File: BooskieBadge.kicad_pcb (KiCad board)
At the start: 2 copper layers, 53 parts, among them J1 TC2030, J2 SFV24R-2STE1HLF, Q1 Si1308EDL, U1 nRF52840, Y1 32MHz

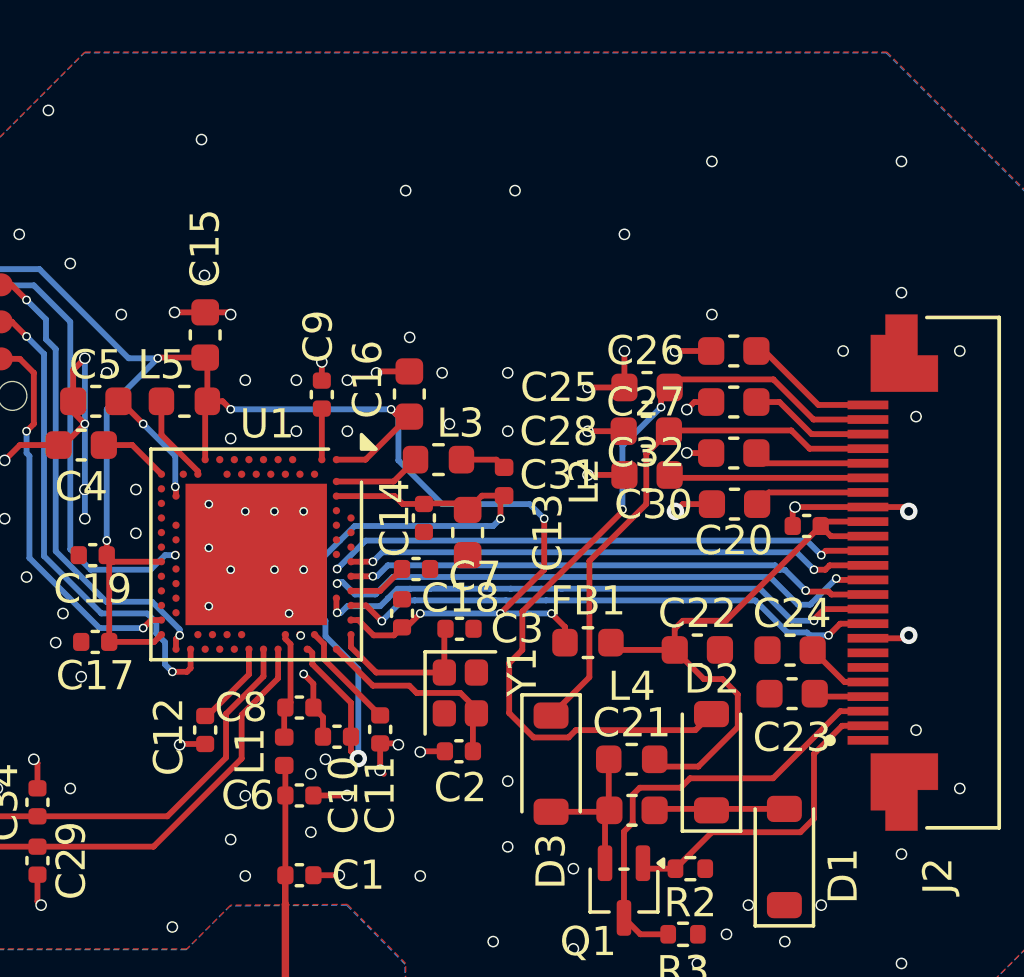
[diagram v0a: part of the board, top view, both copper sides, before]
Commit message: cleaned up some grounds
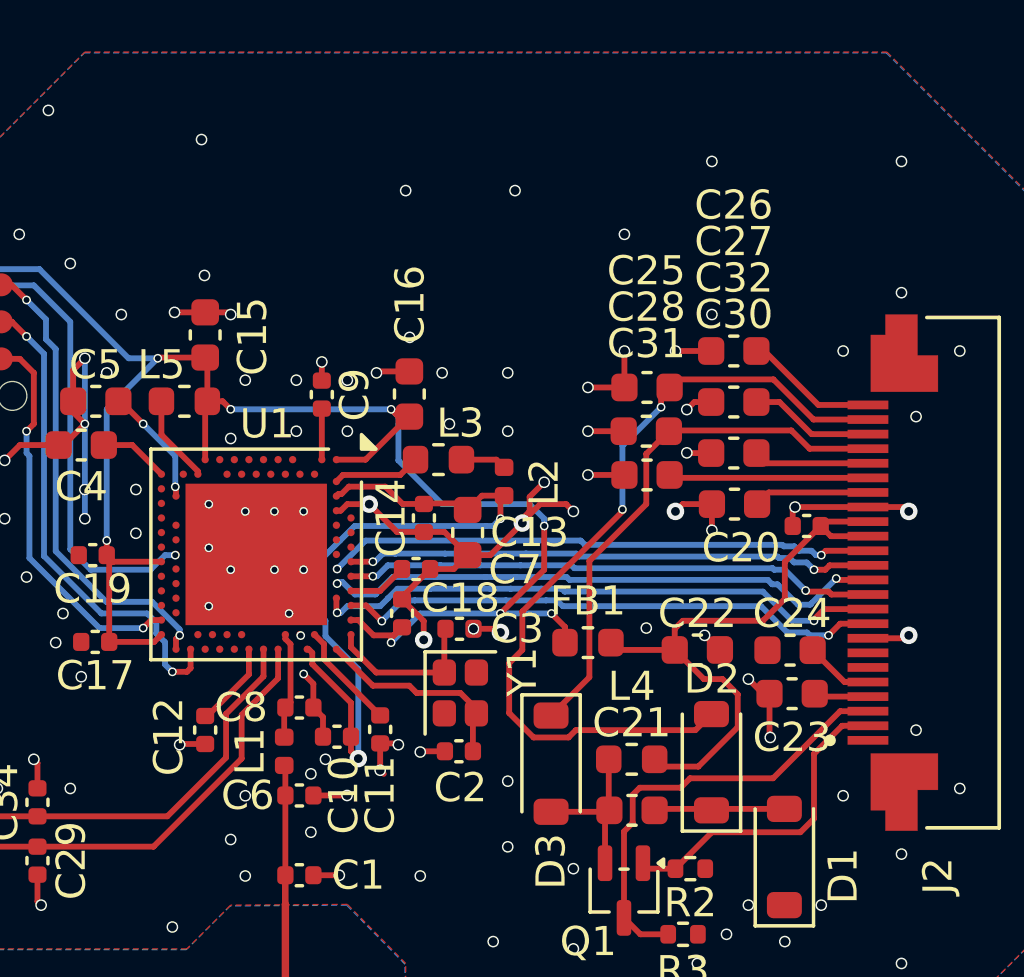
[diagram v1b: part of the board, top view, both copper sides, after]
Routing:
- net GND: track 46.4 -> 67.6 mm, vias 109 -> 122
- net VDD: track 58.9 -> 60.1 mm
- net +3V3: track 20.3 -> 21.0 mm

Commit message: screwing around with ports and stuff
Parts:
- added BT1: Battery_Cell, BooskieBadge:BAT_HOLDER_2032SMD, F.Cu at (97.0, 154.1)
- added J3: USB_C_Receptacle_PCB_Edge, BooskieBadge:USB_C_PCB_receptacle_24pin_1mm-cutout, F.Cu at (107.8, 119.3)
- added J4: USB_A_PCB_Edge_receptacle, BooskieBadge:USB_A_PCB_Edge_receptacle, F.Cu at (92.8, 120.8)
- added R1: 5.1k, Resistor_SMD:R_0402_1005Metric, F.Cu at (103.7, 125.3)
- added R4: 5.1k, Resistor_SMD:R_0402_1005Metric, F.Cu at (103.7, 127.2)
- added U2: USBLC6-2P6, Package_TO_SOT_SMD:SOT-666, F.Cu at (89.3, 129.2)
- added U3: SAOV1.69BIS, BooskieBadge:Simple_Addon_v2-BADGE-2x3, F.Cu at (127.2, 124.0)
- moved AE2 10.3 mm to (90.0, 137.8)
- moved J1 8.50 mm to (108.4, 153.8)
- moved C35 5.09 mm to (106.0, 162.8), turned to 90 degrees
- moved C29 1.28 mm to (110.1, 165.0)
- moved C34 1.28 mm to (110.1, 163.0)
- moved C33 1.17 mm to (106.0, 165.0), turned to -90 degrees
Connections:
- U1 pad A10: unconnected-(U1-AIN5/P0.29-PadA10) -> Net-(U1-AIN5/P0.29)
- U1 pad AD4: unconnected-(U1-D--PadAD4) -> /D-
- U1 pad AD6: unconnected-(U1-D+-PadAD6) -> /D+
- U1 pad B11: unconnected-(U1-AIN4/P0.28-PadB11) -> Net-(U1-AIN4/P0.28)
- U1 pad G1: unconnected-(U1-P0.26-PadG1) -> /SDA
- U1 pad H2: unconnected-(U1-P0.27-PadH2) -> /SCL
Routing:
- net Net-(U1-NFC1/P0.09): track 41.6 -> 55.0 mm
- net Net-(U1-NFC2/P0.10): track 25.5 -> 36.2 mm
- net /~{RST}: track 17.8 -> 7.99 mm
- net /SWCLK: track 16.9 -> 8.72 mm
- net /SWDIO: track 16.2 -> 9.69 mm, vias 2 -> 0
- net /SWO: track 13.4 -> 7.00 mm
- net GND: track 67.6 -> 72.2 mm, vias 122 -> 129
- net VDD: track 60.1 -> 58.9 mm, vias 9 -> 8
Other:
- board outline added: 79 x 38.5 mm

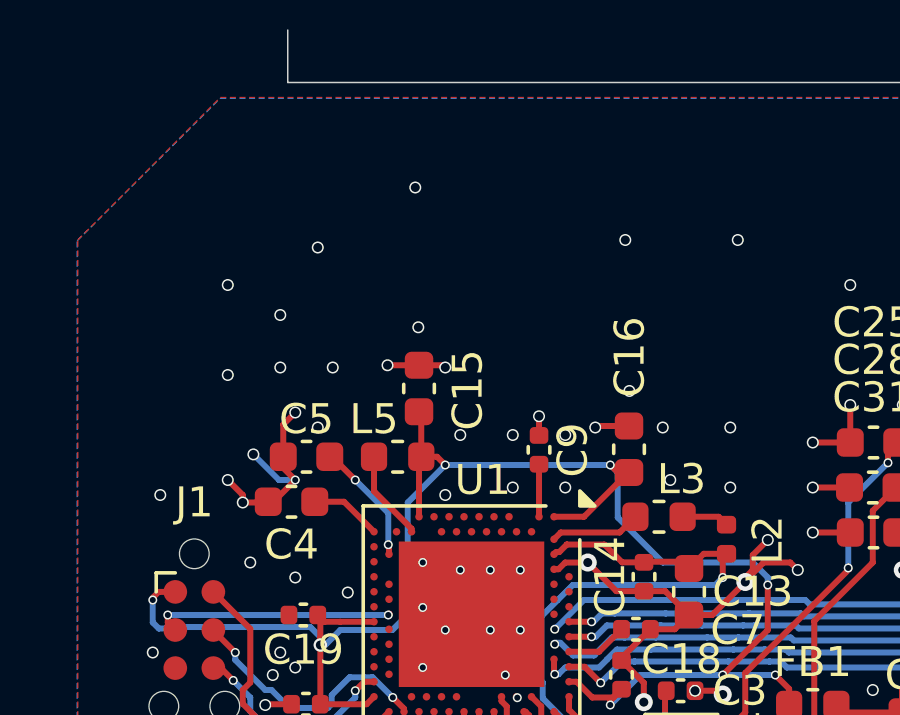
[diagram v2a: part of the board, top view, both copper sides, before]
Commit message: rtc crystal
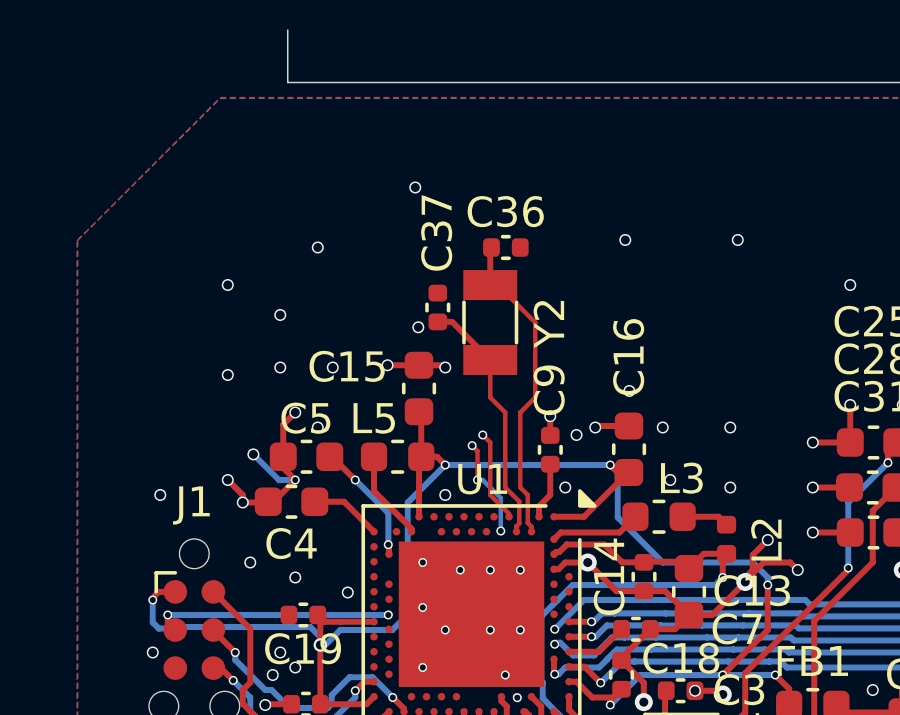
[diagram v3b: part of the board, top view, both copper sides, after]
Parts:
- added C36: 12pF, Capacitor_SMD:C_0402_1005Metric, F.Cu at (118.8, 141.0)
- added C37: 12pF, Capacitor_SMD:C_0402_1005Metric, F.Cu at (116.5, 143.0)
- added Y2: 32.768 kHz, Crystal:Crystal_SMD_3215-2Pin_3.2x1.5mm, F.Cu at (118.2, 143.5)
- moved C9 0.38 mm to (120.2, 147.7)
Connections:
- U1 pad D2: unconnected-(U1-XL1/P0.00-PadD2) -> Net-(U1-XL1/P0.00)
- U1 pad F2: unconnected-(U1-XL2/P0.01-PadF2) -> Net-(U1-XL2/P0.01)
- Y1 pad 2: Net-(U1-XC1) -> unconnected-(Y1-G-Pad2)
- Y1 pad 3: (no net) -> Net-(U1-XC1)
- Y1 pad 4: (no net) -> unconnected-(Y1-G-Pad2)_1
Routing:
- net Net-(U1-XL1/P0.00): track 0.00 -> 10.6 mm
- net Net-(U1-XL2/P0.01): track 0.00 -> 8.44 mm
- net /SCL: track 0.00 -> 3.38 mm, vias 0 -> 3
- net /SDA: track 0.00 -> 3.09 mm, vias 0 -> 1
- net GND: vias 129 -> 126

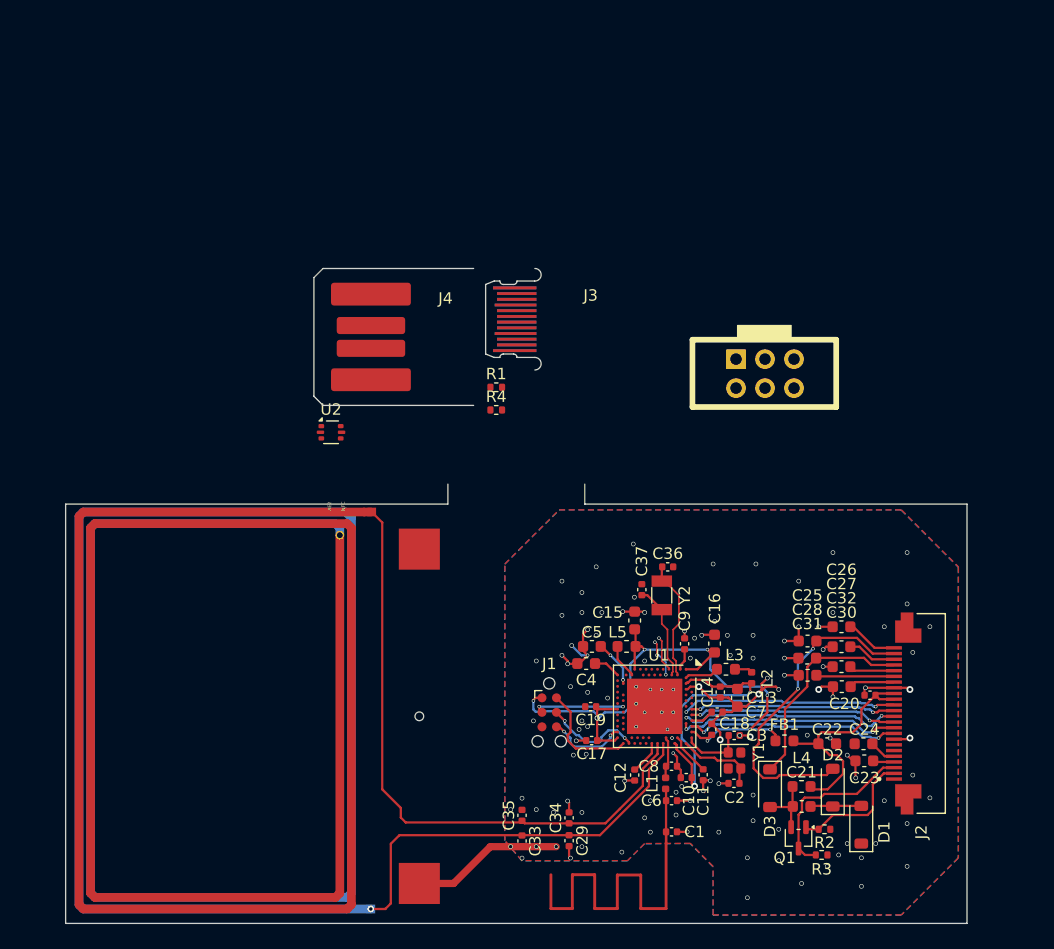
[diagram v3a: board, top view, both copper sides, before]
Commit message: time-of-flight, plus usb, plus li-ion option
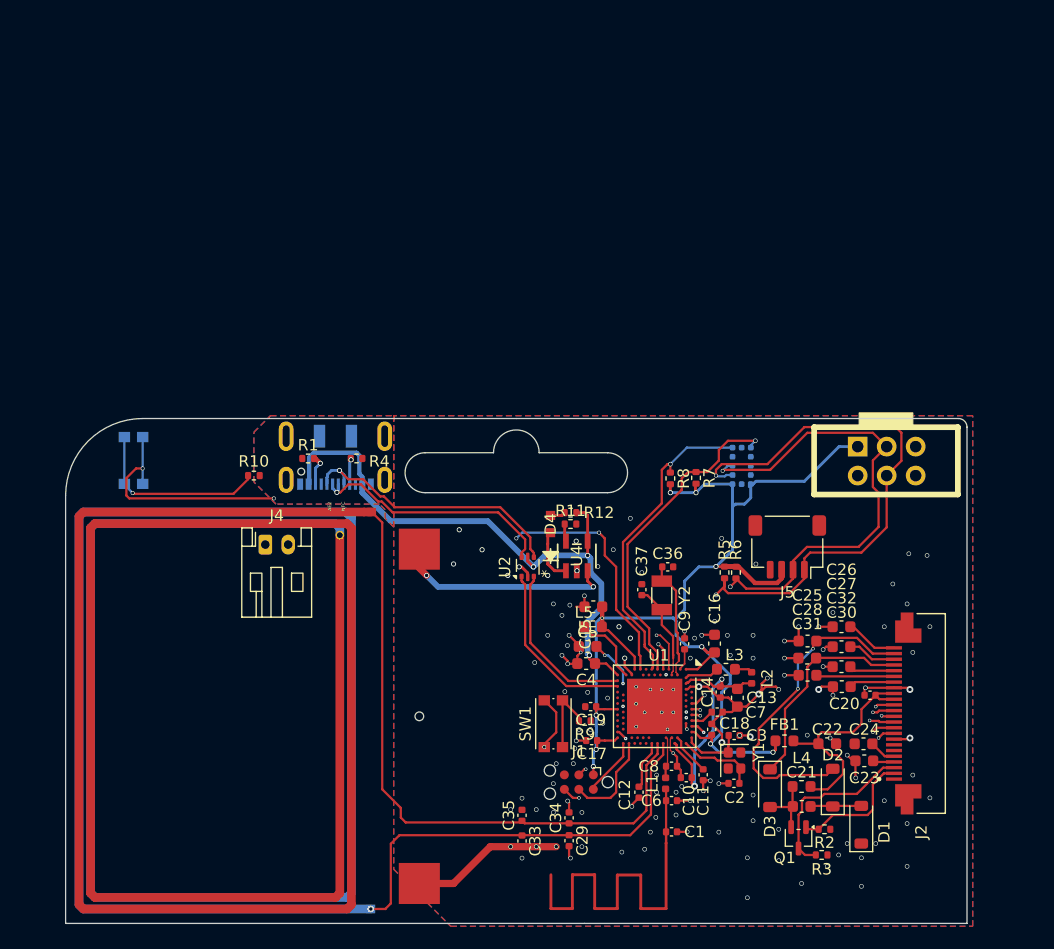
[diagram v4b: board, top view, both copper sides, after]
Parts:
- added D4: LED, BooskieBadge:LED_LB Q39G-L2OO-35-1_OSR, F.Cu at (108.5, 137.2)
- added J5: Conn_01x04, Connector_JST:JST_SH_SM04B-SRSS-TB_1x04-1MP_P1.00mm_Horizontal, F.Cu at (129.2, 139.2)
- added R10: 10k, Resistor_SMD:R_0402_1005Metric, F.Cu at (82.5, 133.0)
- added R11: 5.1k, Resistor_SMD:R_0402_1005Metric, F.Cu at (110.2, 137.2)
- added R12: 5.1k, Resistor_SMD:R_0402_1005Metric, F.Cu at (110.2, 136.2)
- added R5: 10k, Resistor_SMD:R_0402_1005Metric, F.Cu at (123.8, 141.5)
- added R6: 10k, Resistor_SMD:R_0402_1005Metric, F.Cu at (124.8, 141.5)
- added R7: 10k, Resistor_SMD:R_0402_1005Metric, F.Cu at (121.2, 133.2)
- added R8: 10k, Resistor_SMD:R_0402_1005Metric, F.Cu at (119.0, 133.2)
- added R9: 10k, Resistor_SMD:R_0402_1005Metric, F.Cu at (111.5, 154.5)
- added SW1: RST, Button_Switch_SMD:SW_Push_1P1T_NO_CK_KMR2, F.Cu at (108.8, 154.8)
- added SW2: USR, Button_Switch_SMD:SW_Push_1P1T_NO_CK_KMR2, B.Cu at (72.0, 131.7)
- added U4: MCP73831T-2ACI/OT, BooskieBadge:SOT-23-5_MC_MCH, F.Cu at (110.8, 140.0)
- added U5: VL53L1CXV0FY1, Sensor_Distance:ST_VL53L1x, B.Cu at (125.2, 132.2)
- J3: value USB_C_Receptacle_PCB_Edge -> USB_C_Receptacle_USB2.0_16P; footprint BooskieBadge:USB_C_PCB_receptacle_24pin_1mm-cutout -> Connector_USB:USB_C_Receptacle_JAE_DX07S016JA1R1500; moved to B.Cu
- J4: value USB_A_PCB_Edge_receptacle -> JST_PH; footprint BooskieBadge:USB_A_PCB_Edge_receptacle -> Connector_JST:JST_PH_S2B-PH-K_1x02_P2.00mm_Horizontal
- moved J3 21.4 mm to (89.7, 130.7)
- moved U2 20.9 mm to (106.5, 141.0), turned to 90 degrees
- moved J4 20.4 mm to (83.5, 139.1)
- moved R1 17.6 mm to (87.2, 131.5)
- moved U3 13.1 mm to (137.9, 131.7)
- moved R4 13.0 mm to (91.5, 131.5), turned to 180 degrees
- moved J1 6.64 mm to (111.0, 159.9), turned to 180 degrees
- moved C15 3.82 mm to (112.2, 144.5), turned to 180 degrees
- moved L5 3.42 mm to (112.2, 146.2)
- moved C12 1.55 mm to (116.2, 160.8)
- moved C5 0.38 mm to (111.8, 148.0)
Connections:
- J4 pad 1: VBUS -> +BATT
- J4 pad 2: /D_N -> GND
- L5 pad 2: +BATT -> Net-(U1-DCCH)
- U1 pad A10: Net-(U1-AIN5/P0.29) -> unconnected-(U1-AIN5/P0.29-PadA10)
- U1 pad A12: unconnected-(U1-AIN0/P0.02-PadA12) -> /SAO_GP2
- U1 pad AB2: unconnected-(U1-DCCH-PadAB2) -> Net-(U1-DCCH)
- U1 pad B11: Net-(U1-AIN4/P0.28) -> unconnected-(U1-AIN4/P0.28-PadB11)
- U1 pad J1: unconnected-(U1-AIN2/P0.04-PadJ1) -> /SAO_GP1
- U1 pad L1: unconnected-(U1-P0.06-PadL1) -> /TOF_SHDN
- U1 pad N1: unconnected-(U1-P0.08-PadN1) -> /TOF_GP1
- U1 pad U1: unconnected-(U1-TRACEDATA1/P0.12-PadU1) -> Net-(U1-TRACEDATA1/P0.12)
- U3 pad 5: Net-(U1-AIN4/P0.28) -> /SAO_GP1
- U3 pad 6: Net-(U1-AIN5/P0.29) -> /SAO_GP2
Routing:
- net Net-(U1-TRACEDATA1/P0.12): track 0.00 -> 64.1 mm, vias 0 -> 4
- net /SCL: track 3.38 -> 59.4 mm
- net /SDA: track 3.09 -> 54.0 mm, vias 1 -> 3
- net VBUS: track 2.39 -> 52.2 mm, vias 0 -> 3
- net VDD: track 58.9 -> 105.9 mm, vias 8 -> 10
- net +BATT: track 3.02 -> 44.4 mm, vias 0 -> 3
- net /SAO_GP1: track 0.00 -> 39.9 mm, vias 0 -> 1
- net /SAO_GP2: track 0.00 -> 33.5 mm, vias 0 -> 1
- net /TOF_SHDN: track 0.00 -> 28.9 mm, vias 0 -> 1
- net /TOF_GP1: track 0.00 -> 27.8 mm, vias 0 -> 1
- net /D_N: track 0.00 -> 24.4 mm, vias 0 -> 1
- net GND: track 72.2 -> 95.8 mm, vias 126 -> 135
- net /D_P: track 0.00 -> 22.1 mm, vias 0 -> 1
- net Net-(R10-Pad2): track 0.00 -> 16.4 mm, vias 0 -> 1
- net /D+: track 0.00 -> 15.7 mm
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- added copper zone on In1.Cu, net GND
- added copper zone on In2.Cu, net GND
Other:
- board size 79 x 38.5 mm -> 79 x 44.2 mm
- copper layers 2 -> 4

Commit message: bit of clean-up
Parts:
- moved AE2 34.2 mm to (91.7, 103.7)
- moved C6 34.2 mm to (120.7, 127.4)
- moved J1 34.2 mm to (112.6, 125.7)
- moved J4 34.2 mm to (85.1, 104.9)
- moved R5 34.2 mm to (125.4, 107.4)
- moved SW2 34.2 mm to (73.6, 97.5)
- moved U3 34.2 mm to (139.5, 97.6)
- moved AE1 34.2 mm to (120.3, 131.1)
- moved BT1 34.2 mm to (98.6, 120.0)
- moved C1 34.2 mm to (120.7, 130.1)
- moved C10 34.2 mm to (122.0, 125.3)
- moved C11 34.2 mm to (123.5, 125.1)
- moved C12 34.2 mm to (117.9, 126.6)
- moved C13 34.2 mm to (126.5, 118.3)
- moved C14 34.2 mm to (125.0, 117.8)
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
